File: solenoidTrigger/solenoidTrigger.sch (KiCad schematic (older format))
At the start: 41 parts, among them J3 CONN_01X03, J4 UF_2_RA, J5 micromatch, J6 CONN_01X03, J7 CONN_01X03, J8 CONN_02X03, Q1 NMOS_CDS16, Q2 NMOS_CDS16, Q3 NMOS_CDS16, Q4 NMOS_CDS16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

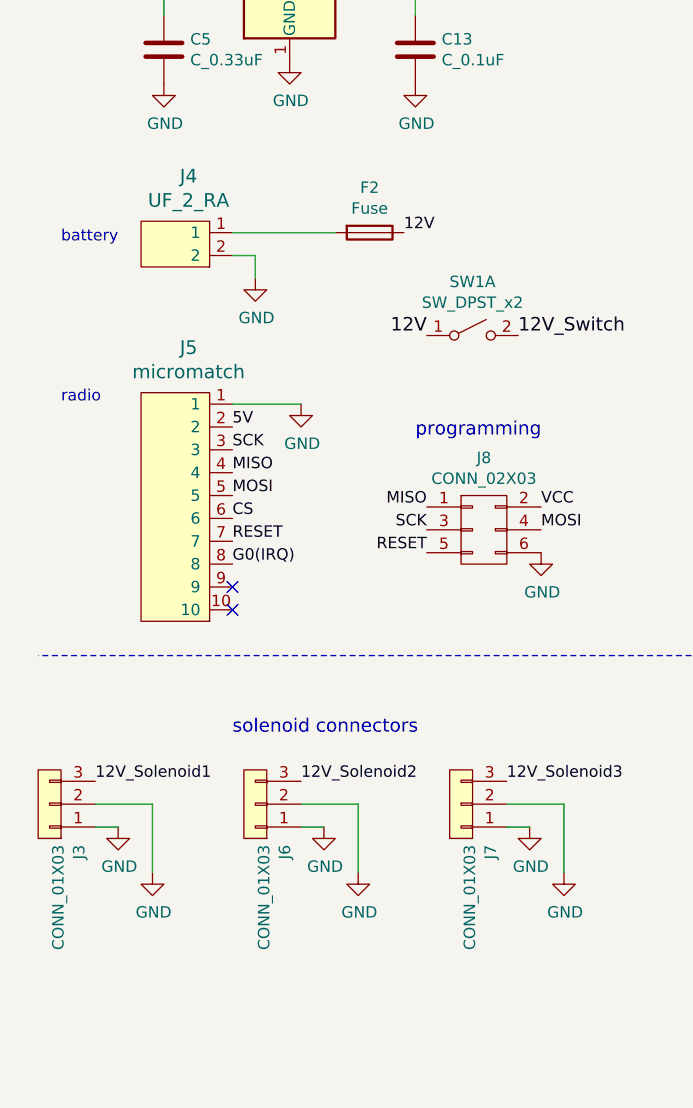
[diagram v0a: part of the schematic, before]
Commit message: created 3 new parts and updated these in the schematic
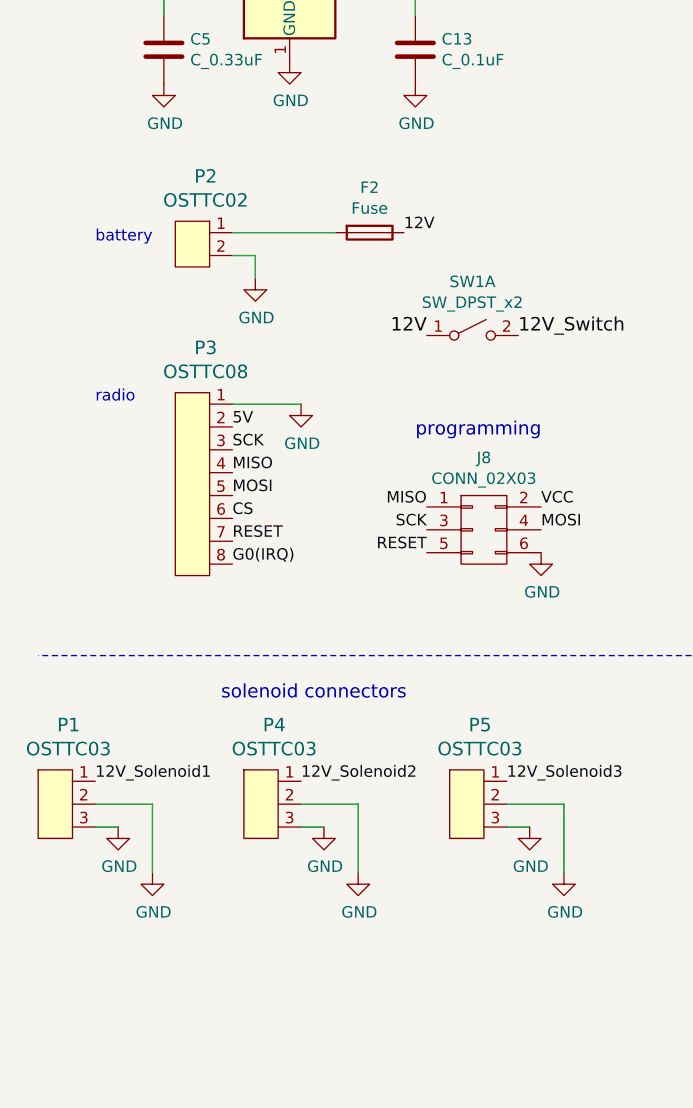
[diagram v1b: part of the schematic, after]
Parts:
- removed J3, J6, J7: CONN_01X03, Pin_Headers:Pin_Header_Straight_1x03_Pitch2.54mm, symbol Rocketry:CONN_01X03
- removed J4: UF_2_RA, footprints:Ultrafit_2_RA, symbol Rocketry:UF_2_RA
- removed J5: micromatch, footprints:micromatch_female_ra_10, symbol solenoidTrigger-rescue:MM_F_RA_10-Rocketry
- added P1, P4, P5: OSTTC03, footprints:OSTTC030162, symbol Rocketry:OSTTC03
- added P2: OSTTC02, footprints:OSTTC02, symbol Rocketry:OSTTC02
- added P3: OSTTC08, footprints:OSTTC080162, symbol Rocketry:OSTTC08
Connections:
- net 12V_Solenoid1: now also P1.1
- net 12V_Solenoid2: now also P4.1
- net 12V_Solenoid3: now also P5.1
- net CS: now also P3.6
- net G0(IRQ): now also P3.8
- net GND: now also P1.2, P1.3, P2.2, P3.1, P4.2, P4.3, P5.2, P5.3
- net MISO: now also P3.4
- net MOSI: now also P3.5
- net RESET: now also P3.7
- net SCK: now also P3.3
- net VCC: now also P3.2
- net at F2.2: now also P2.1
- no-connect marks 11 -> 9
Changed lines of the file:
@@
 $EndDescr
-$Comp
-L solenoidTrigger-rescue:MM_F_RA_10-Rocketry J5
-U 1 1 5D9D113E
-P 1400 9200
-F 0 "J5" H 1358 10547 60  0000 C CNN
-F 1 "micromatch" H 1358 10441 60  0000 C CNN
-F 2 "footprints:micromatch_female_ra_10" H 1200 10300 60  0001 C CNN
-F 3 "http://www.te.com/commerce/DocumentDelivery/DDEController?Action=showdoc&DocId=Customer+Drawing%7F338070%7FG1%7Fpdf%7FEnglish%7FENG_CD_338070_G1.pdf%7F1-338070-0" H 1300 10400 60  0001 C CNN
-F 4 "TE" H 1500 10600 60  0001 C CNN "MFN"
-F 5 "1-338070-0" H 1600 10700 60  0001 C CNN "MPN"
-F 6 "http://www.te.com/usa-en/product-1-338070-0.html#guest-click" H 1400 10500 60  0001 C CNN "PurchasingLink"
-	1    1400 9200
-	1    0    0    -1
-$EndComp
 $Comp
 L power:VCC #PWR0101
@@
 	0    -1   -1   0
 $EndComp
-Text Notes 800  8100 0    50   ~ 0
+Text Notes 950  8100 0    50   ~ 0
 radio
 Text Label 1550 8400 0    50   ~ 0
@@
 Text Label 1550 8300 0    50   ~ 0
 SCK
-$Comp
-L Rocketry:CONN_01X03 J6
-U 1 1 5DABA63C
-P 1600 9850
-F 0 "J6" V 1421 10028 50  0000 L CNN
-F 1 "CONN_01X03" V 1512 10028 50  0000 L CNN
-F 2 "Pin_Headers:Pin_Header_Straight_1x03_Pitch2.54mm" H 1600 8650 50  0001 C CNN
-F 3 "https://www.mouser.com/datasheet/2/181/M20-999-1218971.pdf" H 1600 8650 50  0001 C CNN
-F 4 "Mouser" H 1600 9850 60  0001 C CNN "MFN"
-F 5 "855-M20-9990346" H 1600 9850 60  0001 C CNN "MPN"
-F 6 "https://www.mouser.com/ProductDetail/Harwin/M20-9990346?qs=sGAEpiMZZMs%252bGHln7q6pmzlZUuX%2f53qj1ROyRKct5o4%3d" H 2000 10450 60  0001 C CNN "PurchasingLink"
-	1    1600 9850
-	-1   0    0    1
-$EndComp
-$Comp
-L Rocketry:CONN_01X03 J7
-U 1 1 5DAF073C
-P 2500 9850
-F 0 "J7" V 2321 10028 50  0000 L CNN
-F 1 "CONN_01X03" V 2412 10028 50  0000 L CNN
-F 2 "Pin_Headers:Pin_Header_Straight_1x03_Pitch2.54mm" H 2500 8650 50  0001 C CNN
-F 3 "https://www.mouser.com/datasheet/2/181/M20-999-1218971.pdf" H 2500 8650 50  0001 C CNN
-F 4 "Mouser" H 2500 9850 60  0001 C CNN "MFN"
-F 5 "855-M20-9990346" H 2500 9850 60  0001 C CNN "MPN"
-F 6 "https://www.mouser.com/ProductDetail/Harwin/M20-9990346?qs=sGAEpiMZZMs%252bGHln7q6pmzlZUuX%2f53qj1ROyRKct5o4%3d" H 2900 10450 60  0001 C CNN "PurchasingLink"
-	1    2500 9850
-	-1   0    0    1
-$EndComp
 $Comp
 L power:GND #PWR0102
@@
 Check:\n   - Do the net labels work as intended, or do they not connect in the \n     correct order right now with how I have it set up?\n
 $Comp
-L Rocketry:CONN_01X03 J3
-U 1 1 5DC3C97D
-P 700 9850
-F 0 "J3" V 521 10028 50  0000 L CNN
-F 1 "CONN_01X03" V 612 10028 50  0000 L CNN
-F 2 "Pin_Headers:Pin_Header_Straight_1x03_Pitch2.54mm" H 700 8650 50  0001 C CNN
-F 3 "https://www.mouser.com/datasheet/2/181/M20-999-1218971.pdf" H 700 8650 50  0001 C CNN
-F 4 "Mouser" H 700 9850 60  0001 C CNN "MFN"
-F 5 "855-M20-9990346" H 700 9850 60  0001 C CNN "MPN"
-F 6 "https://www.mouser.com/ProductDetail/Harwin/M20-9990346?qs=sGAEpiMZZMs%252bGHln7q6pmzlZUuX%2f53qj1ROyRKct5o4%3d" H 1100 10450 60  0001 C CNN "PurchasingLink"
-	1    700  9850
-	-1   0    0    1
-$EndComp
-$Comp
 L power:GND #PWR0116
 U 1 1 5DC3C983
@@
 Text Label 2300 7350 0    50   ~ 0
 12V
-Wire Wire Line
-	1550 7350 2000 7350
-Text Notes 800  7400 0    50   ~ 0
+Text Notes 950  7400 0    50   ~ 0
 battery
 $Comp
@@
 Wire Wire Line
 	1650 7450 1650 7550
-Wire Wire Line
-	1550 7450 1650 7450
-$Comp
-L Rocketry:UF_2_RA J4
-U 1 1 5DDAA094
-P 1300 7400
-F 0 "J4" H 1358 7697 60  0000 C CNN
-F 1 "UF_2_RA" H 1358 7591 60  0000 C CNN
-F 2 "footprints:Ultrafit_2_RA" H 1200 7450 60  0001 C CNN
-F 3 "https://www.molex.com/pdm_docs/sd/1723101302_sd.pdf" H 1300 7550 60  0001 C CNN
-F 4 "DK" H 1500 7750 60  0001 C CNN "MFN"
-F 5 "WM11825-ND " H 1600 7850 60  0001 C CNN "MPN"
-F 6 "https://www.digikey.com/product-detail/en/molex-llc/1723101302/WM11825-ND/5360290" H 1400 7650 60  0001 C CNN "PurchasingLink"
-	1    1300 7400
-	1    0    0    -1
-$EndComp
 $Comp
 L Device:Fuse F2
@@
 Text Notes 2350 8250 0    59   ~ 0
 programming
-Text Notes 1550 9550 0    59   ~ 0
+Text Notes 1500 9400 0    59   ~ 0
 solenoid connectors
 $Comp
@@
 Text Notes 1000 2950 0    59   ~ 0
 Check that no connects are correct\n\nChange library of:\n- fuse\n- solenoid connectors
-NoConn ~ 1550 8900
-NoConn ~ 1550 9000
 Text Label 5400 7250 0    50   ~ 0
 12V_Switch
@@
 Wire Notes Line
 	3600 5550 3600 11000
+$Comp
+L Rocketry:OSTTC03 P1
+U 1 1 5DE79A1A
+P 850 9600
+F 0 "P1" H 833 9696 59  0000 C CNN
+F 1 "OSTTC03" H 833 9591 59  0000 C CNN
+F 2 "footprints:OSTTC030162" H 750 9450 59  0001 C CNN
+F 3 "http://www.on-shore.com/wp-content/uploads/OSTTCXX0162.pdf" H 750 9450 59  0001 C CNN
+F 4 "https://www.digikey.com/product-detail/en/on-shore-technology-inc/OSTTC030162/ED2601-ND/614550" H 850 9750 59  0001 C CNN "Purchasing Link"
+F 5 " OSTTC030162 " H 850 9600 59  0001 C CNN "MPN"
+F 6 " ED2601-ND " H 850 9600 59  0001 C CNN "DPN"
+	1    850  9600
+	1    0    0    -1
+$EndComp
+$Comp
+L Rocketry:OSTTC03 P4
+U 1 1 5DE7F97A
+P 1750 9600
+F 0 "P4" H 1733 9696 59  0000 C CNN
+F 1 "OSTTC03" H 1733 9591 59  0000 C CNN
+F 2 "footprints:OSTTC030162" H 1650 9450 59  0001 C CNN
+F 3 "http://www.on-shore.com/wp-content/uploads/OSTTCXX0162.pdf" H 1650 9450 59  0001 C CNN
+F 4 "https://www.digikey.com/product-detail/en/on-shore-technology-inc/OSTTC030162/ED2601-ND/614550" H 1750 9750 59  0001 C CNN "Purchasing Link"
+F 5 " OSTTC030162 " H 1750 9600 59  0001 C CNN "MPN"
+F 6 " ED2601-ND " H 1750 9600 59  0001 C CNN "DPN"
+	1    1750 9600
+	1    0    0    -1
+$EndComp
+$Comp
+L Rocketry:OSTTC03 P5
+U 1 1 5DE85F66
+P 2650 9600
+F 0 "P5" H 2633 9696 59  0000 C CNN
+F 1 "OSTTC03" H 2633 9591 59  0000 C CNN
+F 2 "footprints:OSTTC030162" H 2550 9450 59  0001 C CNN
+F 3 "http://www.on-shore.com/wp-content/uploads/OSTTCXX0162.pdf" H 2550 9450 59  0001 C CNN
+F 4 "https://www.digikey.com/product-detail/en/on-shore-technology-inc/OSTTC030162/ED2601-ND/614550" H 2650 9750 59  0001 C CNN "Purchasing Link"
+F 5 " OSTTC030162 " H 2650 9600 59  0001 C CNN "MPN"
+F 6 " ED2601-ND " H 2650 9600 59  0001 C CNN "DPN"
+	1    2650 9600
+	1    0    0    -1
+$EndComp
+$Comp
+L Rocketry:OSTTC08 P3
+U 1 1 5DE9C768
+P 1450 7900
+F 0 "P3" H 1433 7946 59  0000 C CNN
+F 1 "OSTTC08" H 1433 7841 59  0000 C CNN
+F 2 "footprints:OSTTC080162" H 1350 7700 59  0001 C CNN
+F 3 "http://www.on-shore.com/wp-content/uploads/OSTTCXX0162.pdf" H 1350 7700 59  0001 C CNN
+F 4 "https://www.digikey.com/product-detail/en/on-shore-technology-inc/OSTTC080162/ED2606-ND/614555" H 1450 7950 59  0001 C CNN "Purchasing Link"
+F 5 " OSTTC080162" H 1450 7950 59  0001 C CNN "MPN"
+F 6 "ED2606-ND" H 1450 7950 59  0001 C CNN "DPN"
+	1    1450 7900
+	1    0    0    -1
+$EndComp
+Wire Wire Line
+	1550 7350 2000 7350
+Wire Wire Line
+	1550 7450 1650 7450
+$Comp
+L Rocketry:OSTTC02 P2
+U 1 1 5DEBC83F
+P 1450 7200
+F 0 "P2" H 1433 7296 59  0000 C CNN
+F 1 "OSTTC02" H 1433 7191 59  0000 C CNN
+F 2 "footprints:OSTTC02" H 1350 7050 59  0001 C CNN
+F 3 "http://www.on-shore.com/wp-content/uploads/OSTTCXX0162.pdf" H 1350 7050 59  0001 C CNN
+F 4 "https://www.digikey.com/product-detail/en/on-shore-technology-inc/OSTTC020162/ED2600-ND/614549" H 1450 7200 59  0001 C CNN "Purchasing Link"
+F 5 "OSTTC020162" H 1450 7200 59  0001 C CNN "MPN"
+F 6 " ED2600-ND" H 1450 7200 59  0001 C CNN "DPN"
+	1    1450 7200
+	1    0    0    -1
+$EndComp
 $EndSCHEMATC

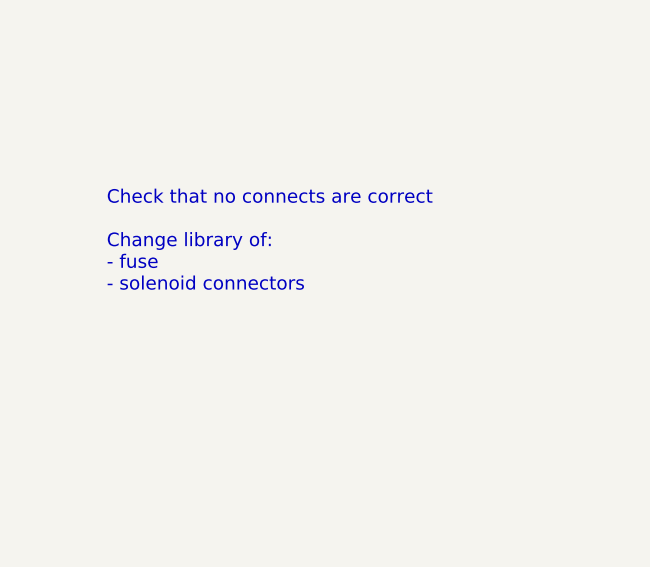
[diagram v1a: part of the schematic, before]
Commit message: Aside from the fact that the fuse and switch footprints need to be added, all the traces for the PCB have been laid out!
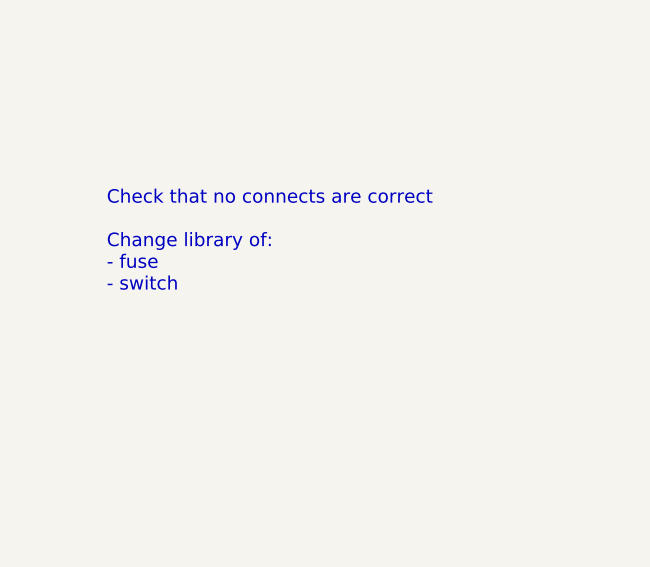
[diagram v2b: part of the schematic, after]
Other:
- note added: "Check that no connects are correct\n\nChange library of:\n- fuse\n- switch"
- note removed: "Check that no connects are correct\n\nChange library of:\n- fuse\n- solenoid connectors"
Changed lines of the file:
@@
 NoConn ~ 10800 7600
 Text Notes 1000 2950 0    59   ~ 0
-Check that no connects are correct\n\nChange library of:\n- fuse\n- solenoid connectors
+Check that no connects are correct\n\nChange library of:\n- fuse\n- switch
 Text Label 5400 7250 0    50   ~ 0
 12V_Switch
